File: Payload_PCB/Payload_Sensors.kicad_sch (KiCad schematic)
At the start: 9 parts, among them J1 Conn_01x06_Pin

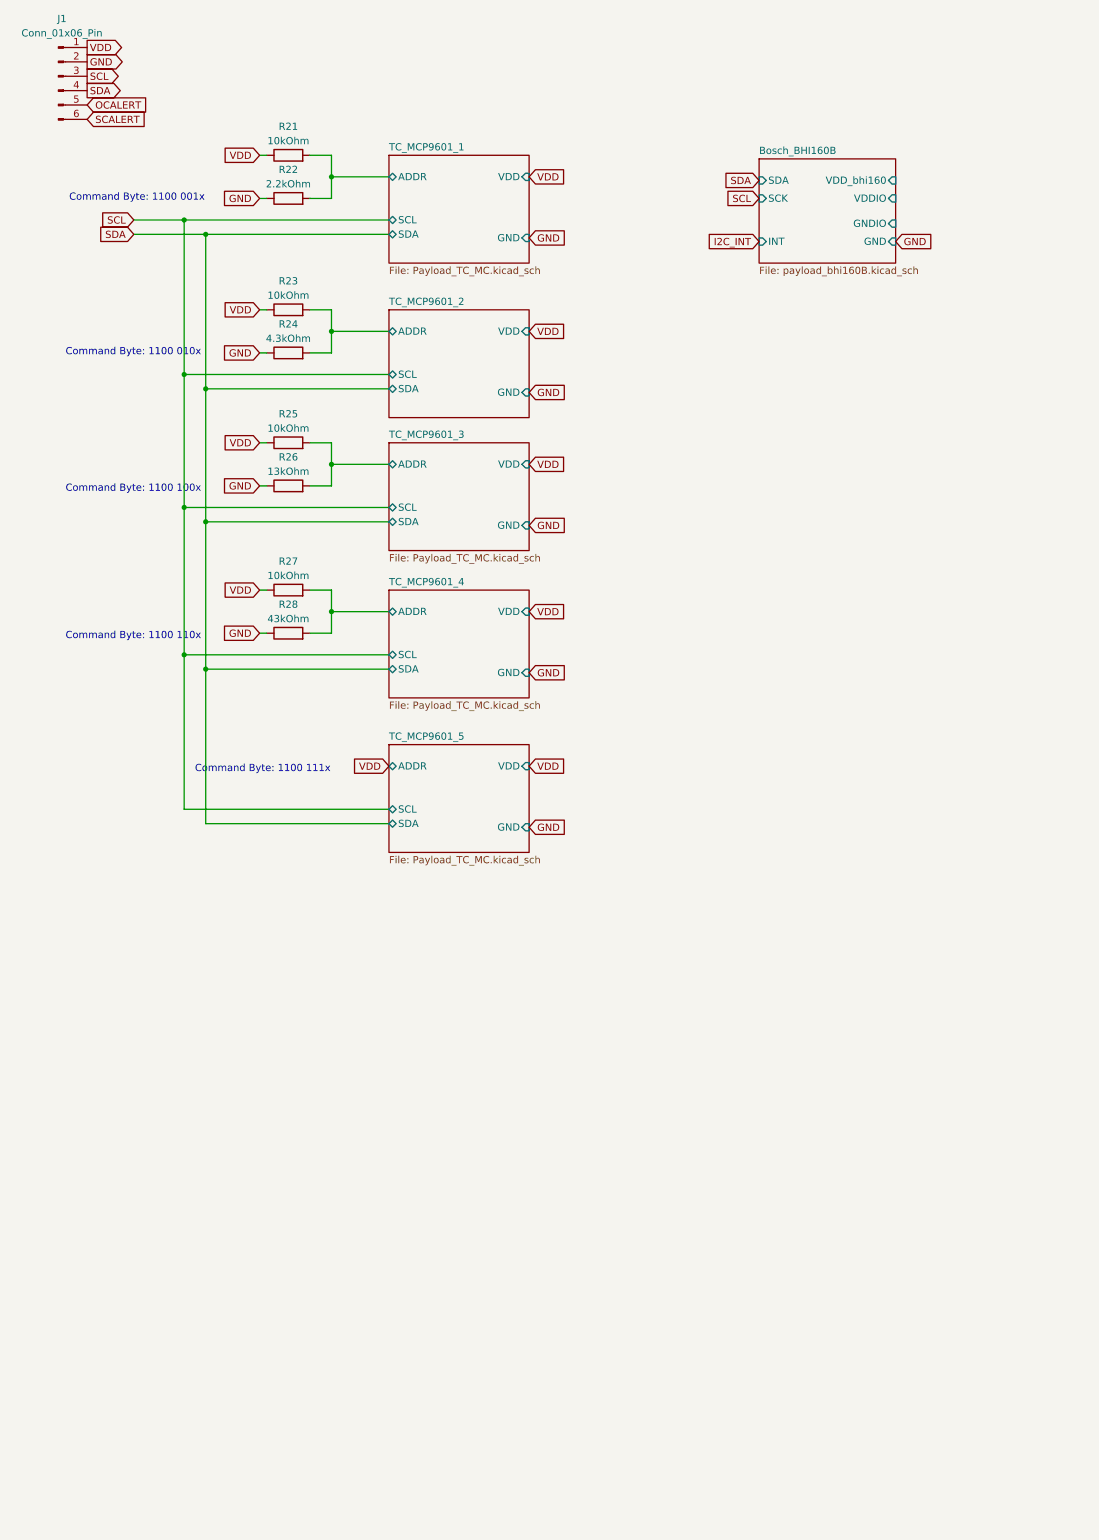
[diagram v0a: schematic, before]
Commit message: Added BHI160 as accelerator and merged two KiCad Projects
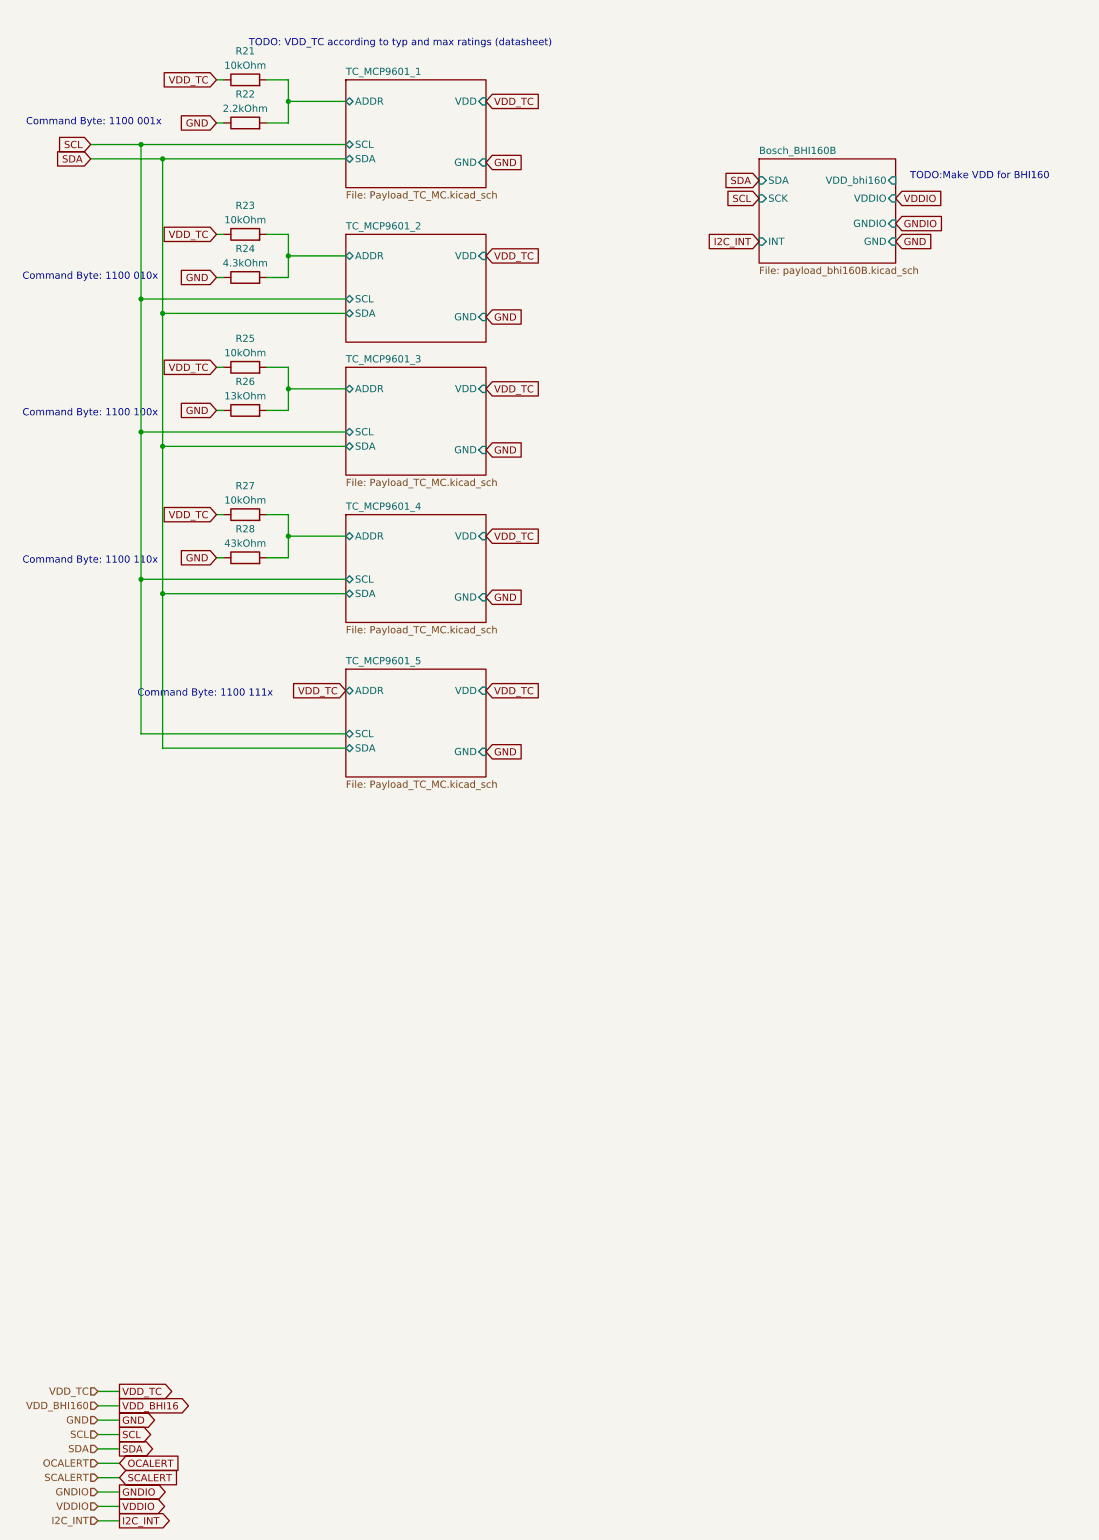
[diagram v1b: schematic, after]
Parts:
- removed J1: Conn_01x06_Pin, symbol Connector:Conn_01x06_Pin
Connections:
- net VDD renamed VDD_TC
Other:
- note added: "TODO: VDD_TC according to typ and max ratings (datasheet)"
- note added: "TODO:Make VDD for BHI160"
- moved on the sheet: R21, R22, R23, R24, R25, R26, R27, R28

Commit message: Minor changes and corrections
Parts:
- renumbered R21 to R17, R22 to R18, R23 to R19, R24 to R20, R25 to R21, R26 to R22, R27 to R23, R28 to R24

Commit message: Added BMI088 and BMP390
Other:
- sheet Bosch_BHI160B renamed Bosch_BMI088
- added sheet Bosch_BMP390 (payload_bmp390.kicad_sch)
- sheet Bosch_BMI088: file payload_bhi160B.kicad_sch -> payload_bmi088.kicad_sch
- sheet Bosch_BMI088 ports: added VDD_bmi088; removed VDD_bhi160
- note added: "TODO:Make VDD for BMI088"
- note removed: "TODO:Make VDD for BHI160"
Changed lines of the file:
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@@
     (effects (font (size 1.27 1.27)) (justify left bottom))
   )
-  (text "TODO:Make VDD for BHI160\n" (at 171.45 44.45 0)
+  (text "TODO:Make VDD for BMI088\n" (at 171.45 44.45 0)
     (effects (font (size 1.27 1.27)) (justify left bottom))
   )
@@
     (stroke (width 0.1524) (type solid))
     (fill (color 0 0 0 0.0000))
-    (property "Sheetname" "Bosch_BHI160B" (at 144.78 39.9284 0)
+    (property "Sheetname" "Bosch_BMI088" (at 144.78 39.9284 0)
       (effects (font (size 1.27 1.27)) (justify left bottom))
     )
-    (property "Sheetfile" "payload_bhi160B.kicad_sch" (at 144.78 59.6396 0)
+    (property "Sheetfile" "payload_bmi088.kicad_sch" (at 144.78 59.6396 0)
       (effects (font (size 1.27 1.27)) (justify left top))
     )
@@
       (effects (font (size 1.27 1.27)) hide)
     )
-    (pin "VDD_bhi160" input (at 168.91 44.45 0)
-      (effects (font (size 1.27 1.27)) (justify right))
-    )
     (pin "GNDIO" input (at 168.91 52.07 0)
       (effects (font (size 1.27 1.27)) (justify right))
@@
     )
     (pin "VDDIO" input (at 168.91 47.625 0)
+      (effects (font (size 1.27 1.27)) (justify right))
+    )
+    (pin "VDD_bmi088" input (at 168.91 44.45 0)
       (effects (font (size 1.27 1.27)) (justify right))
     )
@@
       )
     )
+  )
+  (sheet (at 144.78 71.12) (size 24.765 16.51) (fields_autoplaced)
+    (stroke (width 0.1524) (type solid))
+    (fill (color 0 0 0 0.0000))
+    (property "Sheetname" "Bosch_BMP390" (at 144.78 70.4084 0)
+      (effects (font (size 1.27 1.27)) (justify left bottom))
+    )
+    (property "Sheetfile" "payload_bmp390.kicad_sch" (at 144.78 88.2146 0)
+      (effects (font (size 1.27 1.27)) (justify left top))
+    )
+    (pin "VDDIO" input (at 169.545 76.835 0)
+      (effects (font (size 1.27 1.27)) (justify right))
+    )
+    (pin "SDA" input (at 144.78 74.295 180)
+      (effects (font (size 1.27 1.27)) (justify left))
+    )
+    (pin "INT" input (at 144.78 83.82 180)
+      (effects (font (size 1.27 1.27)) (justify left))
+    )
+    (pin "SCL" input (at 144.78 76.835 180)
+      (effects (font (size 1.27 1.27)) (justify left))
+    )
+    (pin "VDD_bmp390" input (at 169.545 74.295 0)
+      (effects (font (size 1.27 1.27)) (justify right))
+    )
+    (pin "GND" input (at 169.545 83.82 0)
+      (effects (font (size 1.27 1.27)) (justify right))
+    )
+    (instances
+      (project "Payload_PCB"
+        (path "/5c4f9a68-5778-4223-b18a-2e31db8d7d40/d52ba4fa-6dae-452c-85f1-a72652abf275" (page "15"))
+      )
+    )

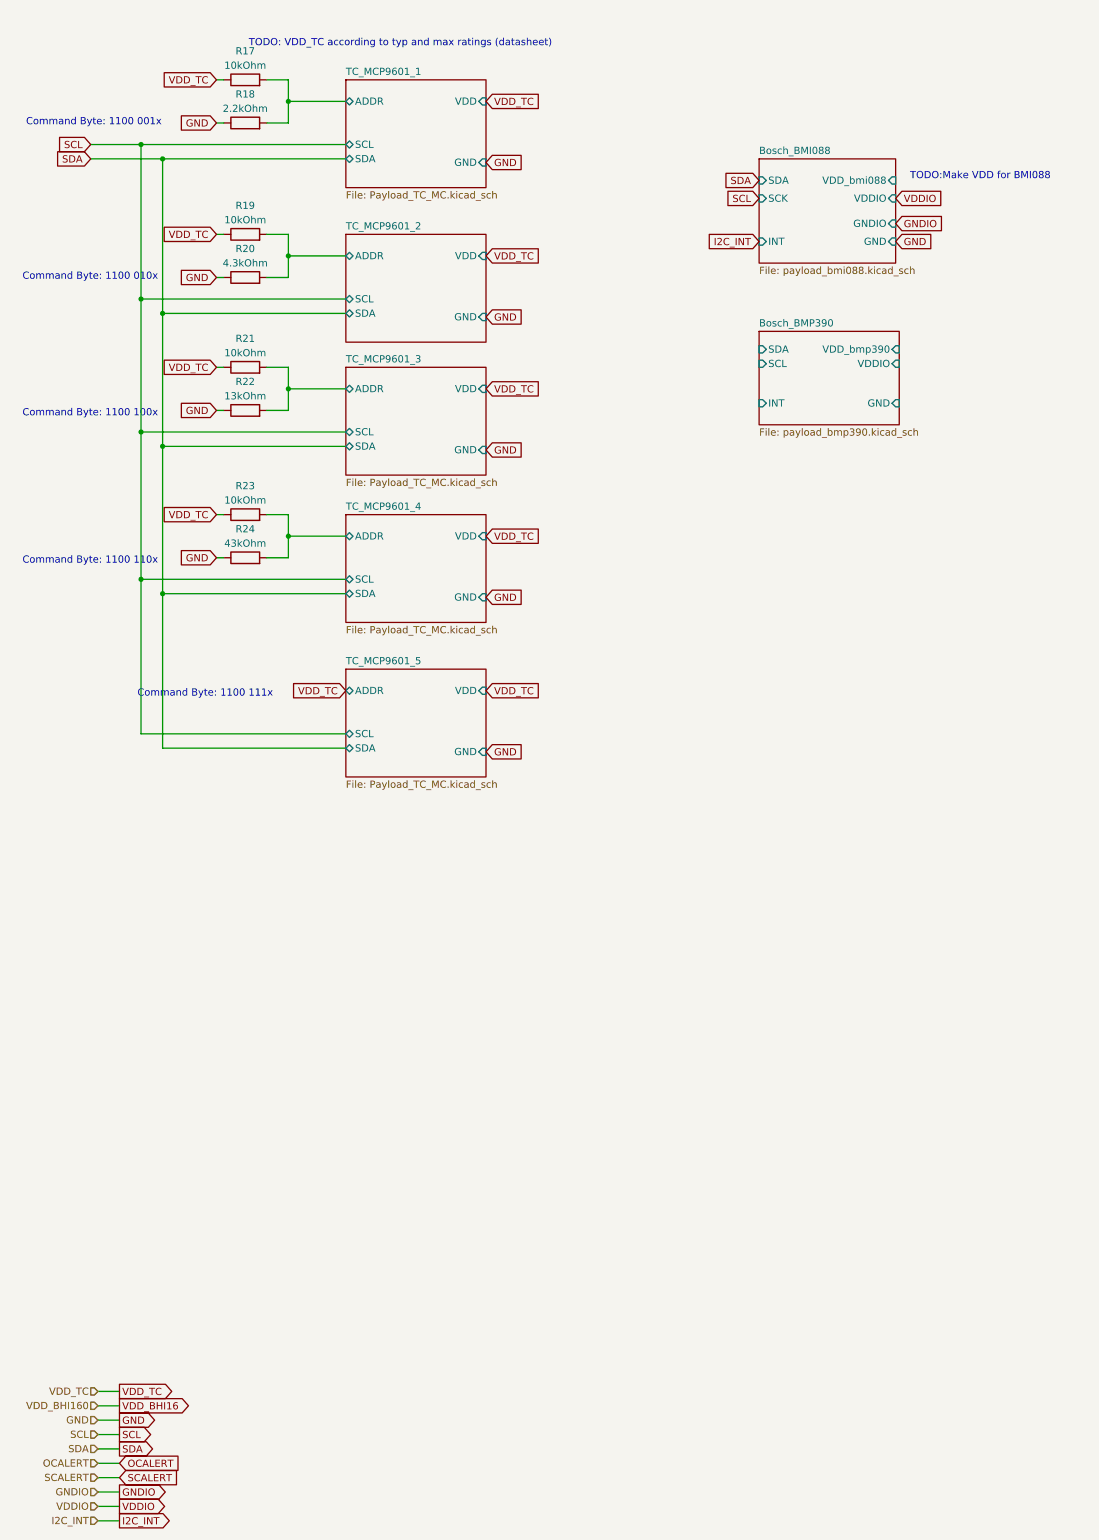
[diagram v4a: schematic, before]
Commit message: Added supply voltage for sensors and changed Radio Silence location
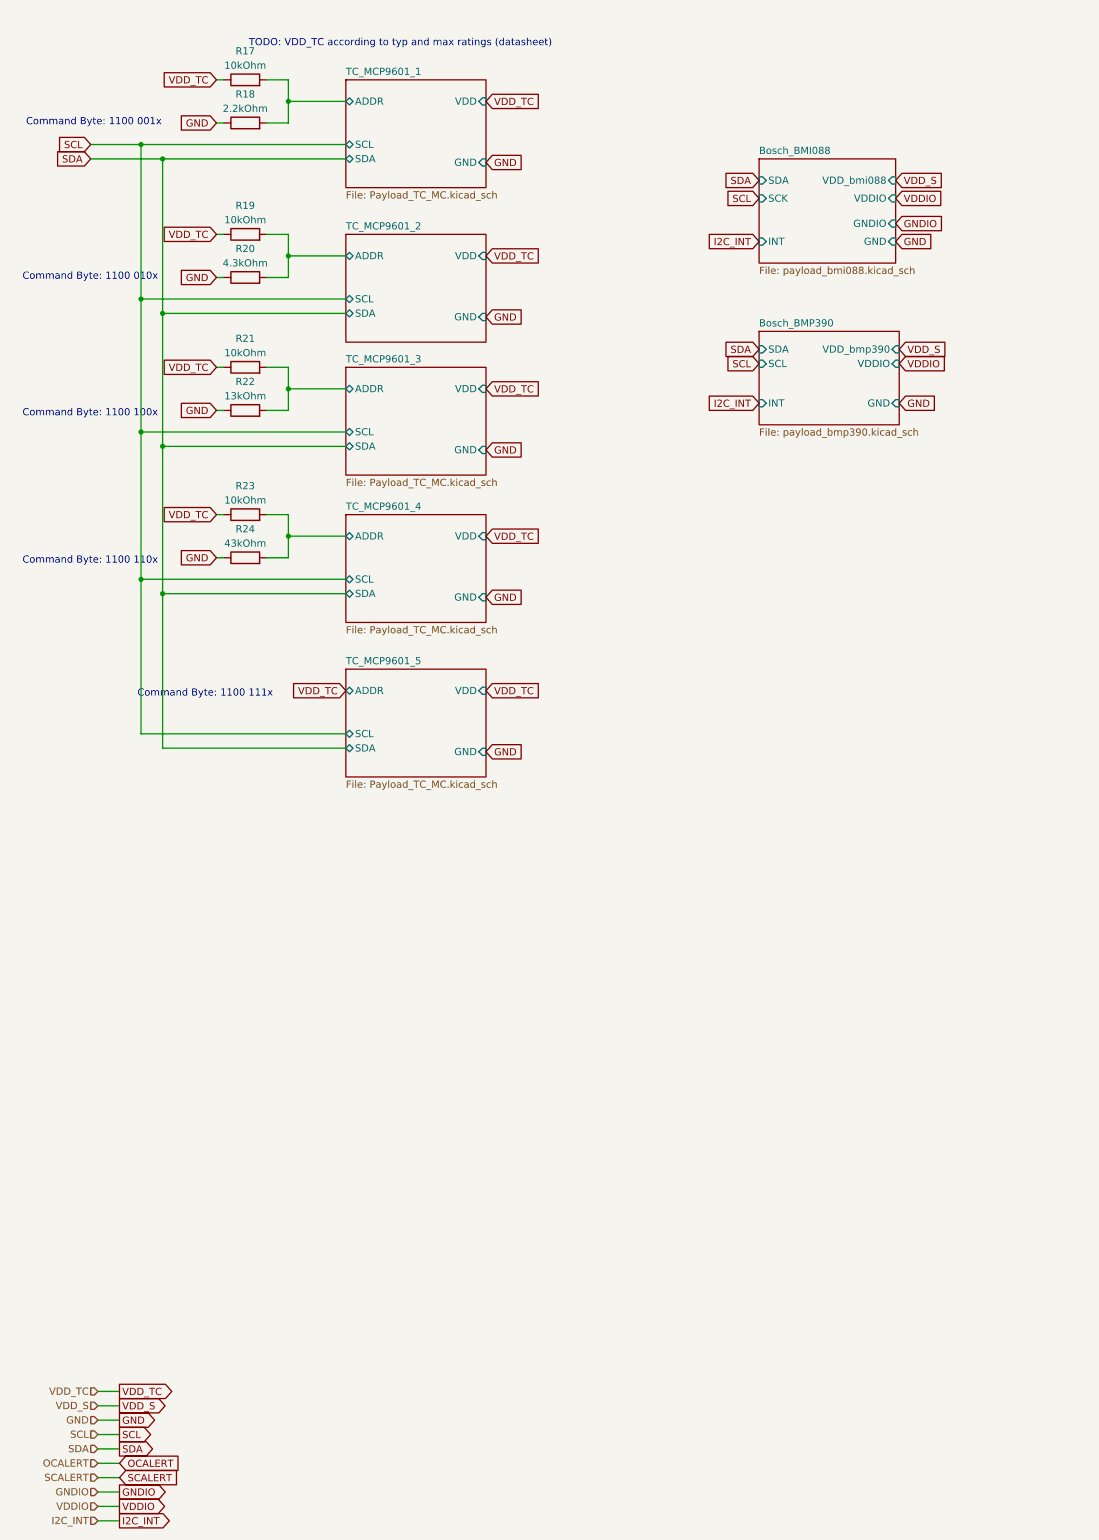
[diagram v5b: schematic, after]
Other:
- note removed: "TODO:Make VDD for BMI088"
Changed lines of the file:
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@@
-    (effects (font (size 1.27 1.27)) (justify left bottom))
-  )
-  (text "TODO:Make VDD for BMI088\n" (at 171.45 44.45 0)
     (effects (font (size 1.27 1.27)) (justify left bottom))
   )
@@
     )
   )
+  (global_label "VDDIO" (shape input) (at 169.545 76.835 0) (fields_autoplaced)
+    (effects (font (size 1.27 1.27)) (justify left))
+    (property "Intersheetrefs" "${INTERSHEET_REFS}" (at 178.0941 76.835 0)
+      (effects (font (size 1.27 1.27)) (justify left) hide)
+    )
+  )
   (global_label "VDD_TC" (shape input) (at 96.52 57.785 0) (fields_autoplaced)
     (effects (font (size 1.27 1.27)) (justify left))
@@
     )
   )
+  (global_label "SDA" (shape input) (at 144.78 74.295 180) (fields_autoplaced)
+    (effects (font (size 1.27 1.27)) (justify right))
+    (property "Intersheetrefs" "${INTERSHEET_REFS}" (at 138.2267 74.295 0)
+      (effects (font (size 1.27 1.27)) (justify right) hide)
+    )
+  )
   (global_label "VDD_TC" (shape input) (at 48.895 77.47 180) (fields_autoplaced)
     (effects (font (size 1.27 1.27)) (justify right))
@@
     )
   )
+  (global_label "VDD_S" (shape input) (at 169.545 74.295 0) (fields_autoplaced)
+    (effects (font (size 1.27 1.27)) (justify left))
+    (property "Intersheetrefs" "${INTERSHEET_REFS}" (at 178.3359 74.295 0)
+      (effects (font (size 1.27 1.27)) (justify left) hide)
+    )
+  )
   (global_label "GND" (shape input) (at 96.52 41.275 0) (fields_autoplaced)
     (effects (font (size 1.27 1.27)) (justify left))
@@
     )
   )
+  (global_label "VDD_S" (shape input) (at 168.91 44.45 0) (fields_autoplaced)
+    (effects (font (size 1.27 1.27)) (justify left))
+    (property "Intersheetrefs" "${INTERSHEET_REFS}" (at 177.7009 44.45 0)
+      (effects (font (size 1.27 1.27)) (justify left) hide)
+    )
+  )
   (global_label "I2C_INT" (shape input) (at 144.78 55.245 180) (fields_autoplaced)
     (effects (font (size 1.27 1.27)) (justify right))
@@
     )
   )
-  (global_label "VDD_BHI16" (shape output) (at 31.75 260.985 0) (fields_autoplaced)
-    (effects (font (size 1.27 1.27)) (justify left))
-    (property "Intersheetrefs" "${INTERSHEET_REFS}" (at 44.9557 260.985 0)
+  (global_label "SCL" (shape input) (at 144.78 76.835 180) (fields_autoplaced)
+    (effects (font (size 1.27 1.27)) (justify right))
+    (property "Intersheetrefs" "${INTERSHEET_REFS}" (at 138.2872 76.835 0)
+      (effects (font (size 1.27 1.27)) (justify right) hide)
+    )
+  )
+  (global_label "VDD_S" (shape output) (at 31.75 260.985 0) (fields_autoplaced)
+    (effects (font (size 1.27 1.27)) (justify left))
+    (property "Intersheetrefs" "${INTERSHEET_REFS}" (at 40.5409 260.985 0)
       (effects (font (size 1.27 1.27)) (justify left) hide)
     )
@@
     )
   )
+  (global_label "GND" (shape input) (at 169.545 83.82 0) (fields_autoplaced)
+    (effects (font (size 1.27 1.27)) (justify left))
+    (property "Intersheetrefs" "${INTERSHEET_REFS}" (at 176.4007 83.82 0)
+      (effects (font (size 1.27 1.27)) (justify left) hide)
+    )
+  )
   (global_label "VDDIO" (shape output) (at 31.75 278.765 0) (fields_autoplaced)
     (effects (font (size 1.27 1.27)) (justify left))
@@
     )
   )
+  (global_label "I2C_INT" (shape input) (at 144.78 83.82 180) (fields_autoplaced)
+    (effects (font (size 1.27 1.27)) (justify right))
+    (property "Intersheetrefs" "${INTERSHEET_REFS}" (at 134.84 83.82 0)
+      (effects (font (size 1.27 1.27)) (justify right) hide)
+    )
+  )
   (hierarchical_label "VDD_TC" (shape input) (at 27.94 258.445 180) (fields_autoplaced)
     (effects (font (size 1.27 1.27)) (justify right))
@@
     (effects (font (size 1.27 1.27)) (justify right))
   )
-  (hierarchical_label "VDD_BHI160" (shape input) (at 27.94 260.985 180) (fields_autoplaced)
-    (effects (font (size 1.27 1.27)) (justify right))
-  )
+  (hierarchical_label "VDD_S" (shape input) (at 27.94 260.985 180) (fields_autoplaced)
+    (effects (font (size 1.27 1.27)) (justify right))
+  )

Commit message: Added some actual parts
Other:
- title: (none) -> Sensor Modules
- moved on the sheet: R17, R18, R19, R20, R21, R22, R23, R24

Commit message: Change to actual real parts
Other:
- sheet Bosch_BMI088 ports: added none; removed GNDIO
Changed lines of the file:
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@@
-    )
-  )
-  (global_label "GNDIO" (shape input) (at 81.28 212.725 0) (fields_autoplaced)
-    (effects (font (size 1.27 1.27)) (justify left))
-    (property "Intersheetrefs" "${INTERSHEET_REFS}" (at 90.071 212.725 0)
-      (effects (font (size 1.27 1.27)) (justify left) hide)
     )
   )
@@
       (effects (font (size 1.27 1.27)) hide)
     )
-    (pin "GNDIO" input (at 81.28 212.725 0)
-      (effects (font (size 1.27 1.27)) (justify right))
-    )
     (pin "SCK" input (at 57.15 208.28 180)
